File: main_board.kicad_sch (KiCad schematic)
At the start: 13 parts, among them CN2 DF40C-50DP-0.4V, CN20 DF40C-20DP-0.4V, CN5 DF40C-20DP-0.4V, CN7 DF40C-20DP-0.4V, J4 DF40C-100DP-0.4V51, J5 DF40C-100DP-0.4V51, SW1 RESET_L, SW2 PWRON_L, U11 SiP32508DT

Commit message: finished rf sense and io board closure, added audio system with pcm and three spdt switches, made changes tp lte module, added ldo and sd/sim slot, updated m.2/audio schematics, added new mic msop qfn sot footprints, and added a protection system for non EM06-A Cards
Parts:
- removed CN5: DF40C-20DP-0.4V, slate113:CONN-SMD_20P-P0.40_HRS_DF40TC-20DP-0.4V, symbol slate113:DF40C-20DP-0.4V
- added C111, C114, C115, C133, C134, C136, C139: 100nF, symbol Device:C_Small
- added C116, C131, C135, C137, C140: 10µF, symbol Device:C_Small
- added C117, C123: 2.2µF, symbol Device:C_Small
- added C118, C120, C121, C124, C129, C130, C132, C138: 1µF, symbol Device:C_Small
- added C119, C122: 100pF, symbol Device:C_Small
- added C125, C126, C127, C128: 1nF, symbol Device:C_Small
- added CN10: DF40C-40DP-0.4V, slate113:CONN-SMD_DF40C-40DP-0.4V, symbol slate113:DF40C-40DP-0.4V
- added FB6, FB7, FB8, FB9: 600Ω @ 100MHz, symbol Device:FerriteBead_Small
- added LS1, LS2: CES-24205-18-L200, symbol Connector:Conn_01x02_Pin
- added MIC1: MSM381A3729H9CP, slate113:MIC-SMD_4P-L3.8-W3.0-P2.46-S1.70-TR, symbol slate113:MSM381A3729H9CP
- added R67: 33Ω, symbol Device:R_Small
- added R70: 10Ω, symbol Device:R_Small
- added R71, R72, R73: 1kΩ, symbol Device:R_Small
- added R74, R75: 10kΩ, symbol Device:R_Small
- added U47: ES8388, slate113:QFN-28_L4.0-W4.0-P0.45-BL-EP, symbol slate113:ES8388
- added U48, U49: TS5A23157DGSR, slate113:MSOP-10_L3.0-W3.0-P0.50-LS5.0-BL, symbol slate113:TS5A23157DGSR
- added U50, U51: PAM8302AASCR, slate113:MSOP-8_L3.0-W3.0-P0.65-LS5.0-BL, symbol slate113:PAM8302AASCR
- added U52: TPS7A0233PDBVR, slate113:SOT-23-5_L2.9-W1.6-P0.95-LS2.8-BR, symbol slate113:TPS7A0233PDBVR
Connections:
- net FerriteGND_RADIO is gone; now on net FerriteGND_Carrier: CN20.21, CN20.22, CN20.23, CN20.24
- net 1V8: now also C111.1, R71.2, R72.2, U47.2 (DVDD), U47.3 (PVDD), U48.8 (V+), U49.8 (V+)
- net 3V3: now also R73.1
- net CM5_5V: now also C132.2, C136.1, C137.1, C139.1, C140.1, U50.6 (VDD), U51.6 (VDD), U52.1 (IN), U52.3 (EN)
- net CM5_UART_RX: now also J4.95
- net CM5_UART_TX: now also J4.21
- net GND: now also CN2.50, C111.2, C114.2, C115.2, C116.2, C117.2, C118.1, C119.2, C121.1, C122.1, C123.2, C125.2, C126.2, C127.2, C128.2, C131.2, C132.1, C133.2, C134.2, C135.2, C136.2, C137.2, C138.1, C139.2, C140.2, CN10.1, CN10.12, CN10.15, CN10.18, CN10.19, CN10.20, CN10.33, CN10.9, R74.1, R75.1, U47.13 (HPGND), U47.18 (AGND), U47.26 (CE), U47.29 (EP), U47.4 (DGND), U48.3 (GND), U49.3 (GND), U50.4 (IN-), U50.7 (GND), U51.4 (IN-), U51.7 (GND), U52.2 (GND)
- net M2_3V3: now also CN10.2
- net M2_DM: now also CN10.17
- net M2_DP: now also CN10.16
- net M2_PWROFF: now also CN10.3
- net PCIE0_CLKREQ: now also CN10.5
- net PCIE0_PERST: now also CN10.4
- net PCIE0_REFCLKN: now also CN10.8
- net PCIE0_REFCLKP: now also CN10.7
- net PCIE0_RXN: now also CN10.14
- net PCIE0_RXP: now also CN10.13
- net PCIE0_TXN: now also CN10.11
- net PCIE0_TXP: now also CN10.10
- net PCIE0_WAKE: now also CN10.6
- net RADIO_EN: now also J4.27
- net RP_RST: now also J4.25
- net SD_CLK: now also CN10.26
- net SD_CMD: now also CN10.24
- net SD_D0: now also CN10.29
- net SD_D1: now also CN10.28
- net SD_D2: now also CN10.22
- net SD_D3: now also CN10.23
- net SD_PWREN: now also CN10.27
- net WIFI_CTRL: now reaches CN2.45
- net WIFI_CTRL: now also J4.45
- net BLE_CTRL: now reaches CN2.46
- net BLE_CTRL: now also J4.49
- net 5G_SENSE: now reaches CN2.47
- net 5G_SENSE: now also J4.47
- net 2.4G_SENSE: now reaches CN2.48
- net 2.4G_SENSE: now also J4.48
- net BLE_SENSE: now reaches CN2.49
- net BLE_SENSE: now also J4.50
- net AMP_L_SD: now reaches J4.80
- net AMP_L_SD: now also C131.1, C133.1, R74.2, U50.1 (~{SD})
- net AMP_R_SD: now reaches J4.82
- net AMP_R_SD: now also C134.1, C135.1, R75.2, U51.1 (~{SD})
- net CM5_SAI_MCLK: now reaches J4.24
- net CM5_SAI_MCLK: now also R67.1
- net CM5_SAI_SCLK: now reaches J4.26
- net CM5_SAI_SCLK: now also U48.9 (NC1)
- net CM5_SAI_LRCK: now reaches J4.28
- net CM5_SAI_LRCK: now also U48.7 (NC2)
- net CM5_SAI_SDI: now reaches J4.30
- net CM5_SAI_SDI: now also U49.7 (NC2)
- net CM5_SAI_SDO: now reaches J4.34
- net CM5_SAI_SDO: now also U49.9 (NC1)
- net MODEM_AUDIO_EN: now reaches J4.36
- net MODEM_AUDIO_EN: now also CN10.34, U48.1 (IN1), U48.5 (IN2), U49.1 (IN1), U49.5 (IN2)
- new net: C130.1, U50.3 (IN+)
- new net: C120.2, U47.24 (LIN1)
- new net: C118.2, U47.20 (VMID)
- new net: C129.2, U51.3 (IN+)
- new net: R67.2, U47.1 (MCLK)
- new net: C114.1, R70.1, U47.16 (HPVDD)
- new net: C117.1, U47.19 (ADCVREF)
- new net AUDIO_3V3: C115.1, C116.1, C138.2, R70.2, U47.17 (AVDD), U52.5 (OUT)
- new net AUDIO_ASDOUT: U47.8 (ASDOUT), U49.6 (COM2)
- new net AUDIO_DSDIN: U47.6 (DSDIN), U49.10 (COM1)
- new net AUDIO_I2C_SCL: R72.1, U47.28 (CCLK)
- new net AUDIO_I2C_SDA: R71.1, U47.27 (CDATA)
- new net AUDIO_LOUT1: C130.2, U47.12 (LOUT1)
- new net AUDIO_LRCK: U47.7 (LRCK), U48.6 (COM2)
- new net AUDIO_PCM_CLK_F: CN10.21, U48.2 (NO1)
- new net AUDIO_PCM_IN_F: CN10.31, U49.4 (NO2)
- new net AUDIO_PCM_OUT_F: CN10.30, U49.2 (NO1)
- new net AUDIO_PCM_SYNC_F: CN10.32, U48.4 (NO2)
- new net AUDIO_ROUT1: C129.1, U47.11 (ROUT1)
- new net AUDIO_SCLK: U47.5 (SCLK), U48.10 (COM1)
- new net AUDIO_VREF: C121.2, U47.10 (VREF)
- new net MIC_BIAS: C123.1, MIC1.1 (VDD), R73.2
- new net MIC_GND_SENSE: C119.1, MIC1.2 (GND), MIC1.3 (GND), U47.23 (RIN1)
- new net MIC_OUT: C124.1, MIC1.4 (OUT)
- new net MIC_OUT_AC: C120.1, C122.2, C124.2
- new net SD_VDD: CN10.25
- new net SPK_L+: FB6.1, U50.5 (VO+)
- new net SPK_L+_F: C125.1, FB6.2, LS1.1 (Pin_1)
- new net SPK_L-: FB7.1, U50.8 (VO-)
- new net SPK_L-_F: C126.1, FB7.2, LS1.2 (Pin_2)
- new net SPK_R+: FB8.1, U51.5 (VO+)
- new net SPK_R+_F: C127.1, FB8.2, LS2.1 (Pin_1)
- new net SPK_R-: FB9.1, U51.8 (VO-)
- new net SPK_R-_F: C128.1, FB9.2, LS2.2 (Pin_2)
- no-connect marks 114 -> 106
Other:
- note added: "Audio LDO"
- note added: "Ferrite"
- note added: "Stereo Audio Codec Stuff"
- note removed: "Misc"
- moved on the sheet: J4A, J4B

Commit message: finished slateconnect i2c gpio expander, completed led status bar schematic, fixed all drc errors, started assigning footprints and started bom
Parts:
- removed CN20, CN7: DF40C-20DP-0.4V, slate113:CONN-SMD_20P-P0.40_HRS_DF40TC-20DP-0.4V, symbol slate113:DF40C-20DP-0.4V
- added C147, C211, C215, C219: 100nF, Capacitor_SMD:C_0603_1608Metric, symbol Device:C_Small
- added C150, C155: 1µF, Capacitor_SMD:C_0603_1608Metric, symbol Device:C_Small
- added C156: 100pF, Capacitor_SMD:C_0603_1608Metric, symbol Device:C_Small
- added C213: 47µF, symbol Device:C_Small
- added C217: 4.7µF, Capacitor_SMD:C_0603_1608Metric, symbol Device:C_Small
- added CN11: DF40C-30DP-0.4V, slate113:CONN-SMD_30P-P0.40_5001-BM0430-15-00, symbol slate113:DF40C-30DP-0.4V
- added CN19: DF40C-24DP-0.4V, slate113:CONN-SMD_DF40C-24DP-0.4V, symbol slate113:DF40C-24DP-0.4V
- added CN8: DF40C-40DP-0.4V, slate113:CONN-SMD_DF40C-40DP-0.4V, symbol slate113:DF40C-40DP-0.4V
- added FPC1: FPC0.5-24P, slate113:FPC-SMD_P0.50-24P_XJ-FGS, symbol slate113:FPC0.5-24P
- added FPC2: FPC-0.5FX-6PWBH10, slate113:FPC-SMD_FPC-0.5FX-6PWBH10, symbol slate113:FPC-0.5FX-6PWBH10
- added Q4: MMBT3904-C20526, slate113:SOT-23-3_L2.9-W1.3-P1.90-LS2.4-BR, symbol slate113:MMBT3904-C20526
- added R105: 100kΩ, Resistor_SMD:R_0603_1608Metric, symbol Device:R_Small
- added R106, R107: 560Ω, Resistor_SMD:R_0603_1608Metric, symbol Device:R_Small
- added R108, R109, R96: 10kΩ, Resistor_SMD:R_0603_1608Metric, symbol Device:R_Small
- added R97, R98: 4.7kΩ, Resistor_SMD:R_0603_1608Metric, symbol Device:R
- added R99: 200kΩ, Resistor_SMD:R_0603_1608Metric, symbol Device:R_Small
- added U62: PCA9306DCUR, slate113:SSOP-8_L2.0-W2.3-P0.50-LS3.1-BR, symbol slate113:PCA9306DCUR
- added U63: AP2120N-2.8TRG1, slate113:SOT-23-3_L2.9-W1.3-P1.90-LS2.4-BR, symbol slate113:AP2120N-2.8TRG1
- added U66: DF40B-10DS-0.4V, slate113:CONN-SMD_10P-P0.40_DF40B-10DS-0.4V-51, symbol slate113:DF40B-10DS-0.4V
- added U67: SIP32508DT-T1-GE3, slate113:TSOT-23-6_L2.9-W1.6-P0.95-LS2.8-BR, symbol slate113:SIP32508DT-T1-GE3
- added U68: SN74AHCT125PWR, slate113:TSSOP-14_L5.0-W4.4-P0.65-LS6.4-BL, symbol slate113:SN74AHCT125PWR
- added U8: ESD7104MUTAG_C2987068, slate113:DFN-10_L2.5-W1.0-P0.50-BL, symbol slate113:ESD7104MUTAG_C2987068
- C111, C114, C115, C133, C134, C136, C139, C21: footprint (none) -> Capacitor_SMD:C_0603_1608Metric; MPN (none) -> CL10B104KB8NNNC; Manufacturer (none) -> Samsung Electro-Mechanics
- C116, C131, C135, C137, C140: footprint (none) -> Capacitor_SMD:C_0603_1608Metric; MPN (none) -> CL10A106KP8NNNC; Manufacturer (none) -> Samsung Electro-Mechanics
- C117, C123, C19: footprint (none) -> Capacitor_SMD:C_0603_1608Metric; MPN (none) -> CL10B225KA8NNNC; Manufacturer (none) -> Samsung Electro-Mechanics
- C118, C120, C121, C124, C129, C130, C132, C138: footprint (none) -> Capacitor_SMD:C_0603_1608Metric; MPN (none) -> CL10B105KA8NNNC; Manufacturer (none) -> Samsung Electro-Mechanics
- C119, C122: footprint (none) -> Capacitor_SMD:C_0603_1608Metric; MPN (none) -> CL10C101JB8NNNC; Manufacturer (none) -> Samsung Electro-Mechanics
- C125, C126, C127, C128: footprint (none) -> Capacitor_SMD:C_0603_1608Metric; MPN (none) -> CL10B102KB8NNNC; Manufacturer (none) -> Samsung Electro-Mechanics
- J4: MPN (none) -> DF40C-100DP-0.4V51; Manufacturer (none) -> LCSC
- R17: footprint (none) -> Resistor_SMD:R_0603_1608Metric; MPN (none) -> RC0603FR-07100KL; Manufacturer (none) -> Yageo
- R67: footprint (none) -> Resistor_SMD:R_0603_1608Metric; MPN (none) -> RC0603FR-0733RL; Manufacturer (none) -> Yageo
- R70: footprint (none) -> Resistor_SMD:R_0603_1608Metric; MPN (none) -> RC0603FR-0710RL; Manufacturer (none) -> Yageo
- R71, R72, R73: footprint (none) -> Resistor_SMD:R_0603_1608Metric; MPN (none) -> RC0603FR-071KL; Manufacturer (none) -> Yageo
- R74, R75: footprint (none) -> Resistor_SMD:R_0603_1608Metric; MPN (none) -> RC0603FR-0710KL; Manufacturer (none) -> Yageo
- SW1: MPN (none) -> C&K KMR231GLFS; Manufacturer (none) -> C&K
- SW2: MPN (none) -> C&K KMR231GLFS; Manufacturer (none) -> DigiKey
- U11: MPN (none) -> SiP32508DT; Manufacturer (none) -> LCSC
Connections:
- net 1V8: now also CN11.5, FPC1.22, R96.1, R97.2, R98.1, U62.2 (VREF1)
- net 3V3: now also C150.1, CN11.4, CN19.14, CN8.11, FPC1.23, R99.2, U63.3 (VIN)
- net 5V: now also CN19.12
- net BQ_INT: now also CN11.7
- net CM5_5V: now also C215.1, C217.1, C219.1, CN11.2, CN11.3, R109.2, U67.5 (IN), U67.6 (IN), U68.10 (~{3OE}), U68.13 (~{4OE}), U68.14 (VCC)
- net CM5_UART_RX: now also CN19.17
- net CM5_UART_TX: now also CN19.19
- net FerriteGND_Carrier: now also CN10.41, CN10.42, CN10.43, CN10.44, CN11.31, CN11.32, CN11.33, CN11.34, CN19.25, CN19.26, CN19.27, CN19.28
- net GND: now also C147.2, C150.2, C155.1, C156.2, C211.2, C213.2, C215.2, C217.2, C219.2, CN11.1, CN11.11, CN11.12, CN11.6, CN19.10, CN19.11, CN19.16, CN19.18, CN19.20, CN19.24, CN19.9, CN8.1, CN8.2, CN8.3, CN8.4, CN8.41, CN8.42, CN8.43, CN8.44, FPC1.11, FPC1.14, FPC1.17, FPC1.2, FPC1.24, FPC1.25, FPC1.26, FPC1.5, FPC1.8, FPC2.6, FPC2.7, FPC2.8, Q4.2 (E), R105.2, U62.1 (GND), U63.1 (GND), U66.11, U66.12, U66.13, U66.14, U66.2, U66.4, U66.5, U66.8, U67.4 (GND), U68.12 (4A), U68.7 (GND), U68.9 (3A), U8.3, U8.8
- net I2C0_SCL: now also CN11.8, CN8.13, U62.6 (SCL2)
- net I2C0_SDA: now also CN11.9, CN8.12, U62.5 (SDA2)
- net MODEM_AUDIO_EN: now also J4.91; no longer J4.36
- net RADIO_EN: now also J4.89, CN19.13; no longer J4.27
- net RP_RST: now also J4.97, CN19.15; no longer J4.25
- net SD_CLK: no longer CN2.19
- net SD_CMD: no longer CN2.20
- net SD_D0: no longer CN2.21
- net SD_D1: no longer CN2.22
- net SD_D2: no longer CN2.23
- net SD_D3: no longer CN2.24
- net SD_DET: no longer CN2.25
- net SD_PWREN: no longer CN2.18
- net DSI_D0N: now reaches J5.75
- net DSI_D0N: now also FPC1.6
- net DSI_D0P: now reaches J5.77
- net DSI_D0P: now also FPC1.7
- net DSI_D1N: now reaches J5.81
- net DSI_D1N: now also FPC1.12
- net DSI_D1P: now reaches J5.83
- net DSI_D1P: now also FPC1.13
- net DSI_CLKN: now reaches J5.87
- net DSI_CLKN: now also FPC1.9
- net DSI_CLKP: now reaches J5.89
- net DSI_CLKP: now also FPC1.10
- net DSI_D2N: now reaches J5.93
- net DSI_D2N: now also FPC1.15
- net DSI_D3N: now reaches J5.94
- net DSI_D3N: now also FPC1.3
- net DSI_D2P: now reaches J5.95
- net DSI_D2P: now also FPC1.16
- net DSI_D3P: now reaches J5.96
- net DSI_D3P: now also FPC1.4
- net CM5_ACC_RESET_N: now reaches J4.54
- net CM5_ACC_RESET_N: now also CN8.27
- net CM5_ACC_AUX0: now reaches J4.56
- net CM5_ACC_AUX0: now also CN8.28
- net CM5_ACC_MISO: now reaches J4.29
- net CM5_ACC_MISO: now also CN8.24
- net CM5_ACC_CS0_N: now reaches J4.31
- net CM5_ACC_CS0_N: now also CN8.25
- net CM5_ACC_IRQ0: now reaches J4.35
- net CM5_ACC_IRQ0: now also CN8.26
- net LCD_RST_L: now reaches J4.39
- net LCD_RST_L: now also C147.1, FPC1.19, R96.2
- new net: C156.1, R99.1, U62.7 (VREF2), U62.8 (EN)
- new net CM5_ACC_AUX1: CN8.29, J4.36
- new net CM5_ACC_MOSI: CN8.23, J4.27
- new net CM5_ACC_SCK: CN8.22, J4.25
- new net LCD_LED_A: CN11.20, FPC1.21
- new net LCD_LED_K: CN11.21, FPC1.20
- new net LCD_PWM: CN11.19, FPC1.18
- new net LED_5V: C211.1, C213.1, U66.1, U66.10, U66.3, U66.9, U67.1 (OUT), U67.2 (OUT)
- new net LED_BUF_BASE: Q4.1 (B), R108.1
- new net LED_BUF_OE_N: Q4.3 (C), R109.1, U68.1 (~{1OE}), U68.4 (~{2OE})
- new net LED_CLK_3V3: CN19.22, U68.5 (2A)
- new net LED_CLK_5V: R107.1, U68.6 (2Y)
- new net LED_CLK_IN: R107.2, U66.6
- new net LED_DATA_3V3: CN19.21, U68.2 (1A)
- new net LED_DATA_5V: R106.1, U68.3 (1Y)
- new net LED_DATA_IN: R106.2, U66.7
- new net LED_PWR_EN: CN19.23, R105.1, R108.2, U67.3 (EN)
- new net RP_ACC_AUX0: CN19.1, CN8.36
- new net RP_ACC_AUX1: CN19.2, CN8.37
- new net RP_ACC_CS0_N: CN19.6, CN8.33
- new net RP_ACC_IRQ0: CN19.3, CN8.34
- new net RP_ACC_MISO: CN19.5, CN8.32
- new net RP_ACC_MOSI: CN19.8, CN8.31
- new net RP_ACC_RESET_N: CN19.4, CN8.35
- new net RP_ACC_SCK: CN19.7, CN8.30
- new net SC_SEL0: CN8.14
- new net SC_SEL1: CN8.15
- new net SC_SEL2: CN8.16
- new net SC_SEL3: CN8.17
- new net SC_SEL4: CN8.18
- new net SC_SEL5: CN8.19
- new net SC_SEL6: CN8.20
- new net SC_SEL7: CN8.21
- new net TP_2V8: C155.2, FPC2.1, U63.2 (VOUT)
- new net TP_INT_L: FPC2.5, U8.5
- new net TP_RST_L: FPC2.3, U8.2
- new net TP_SCL_1V8: FPC2.2, R98.2, U62.3 (SCL1), U8.1
- new net TP_SDA_1V8: FPC2.4, R97.1, U62.4 (SDA1), U8.4
- new net VBUS: CN11.13, CN11.14, CN11.15, CN8.5, CN8.6, CN8.7
- new net VIN_EXT: CN11.16, CN11.17, CN11.18, CN8.10, CN8.8, CN8.9
- no-connect marks 106 -> 99
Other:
- note added: "2V8 LDO"
- note added: "B2B > Carrier"
- note added: "Buffer"
- note added: "Carrier -> LED Status"
- note added: "Display Clamshell"
- note added: "Level Shifter"
- note added: "MOSFET"
- note added: "Power Distributor"
- note added: "TVS"
- note added: "Touch Clamshell"
- moved on the sheet: J4B

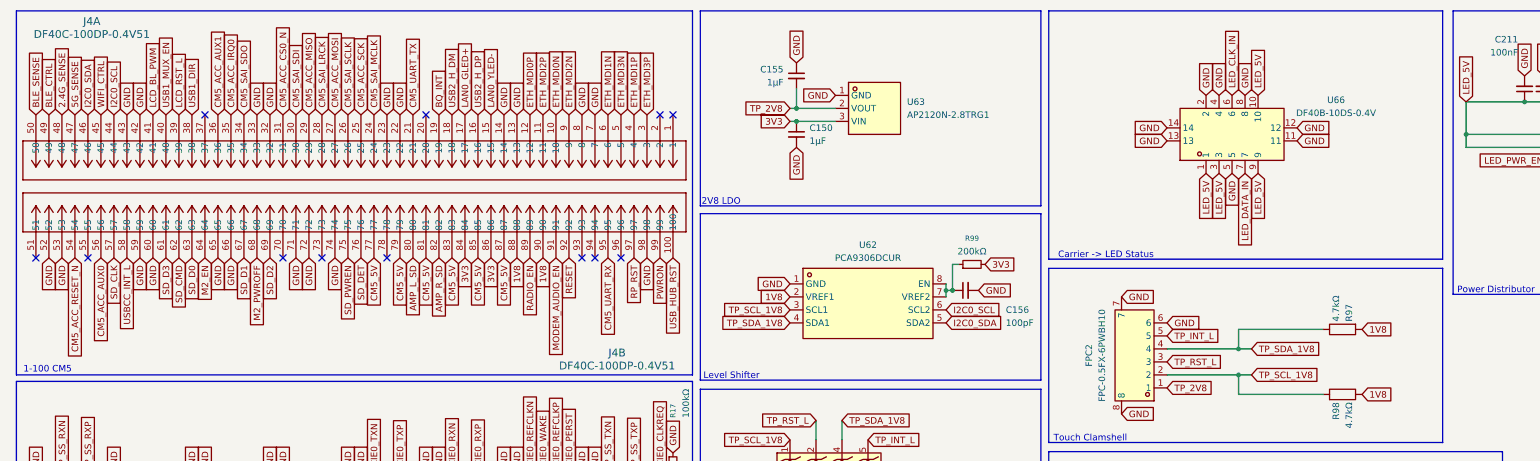
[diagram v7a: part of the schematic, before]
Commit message: assigned footprints and mpns across schematics + added 3d models and footprint libraries
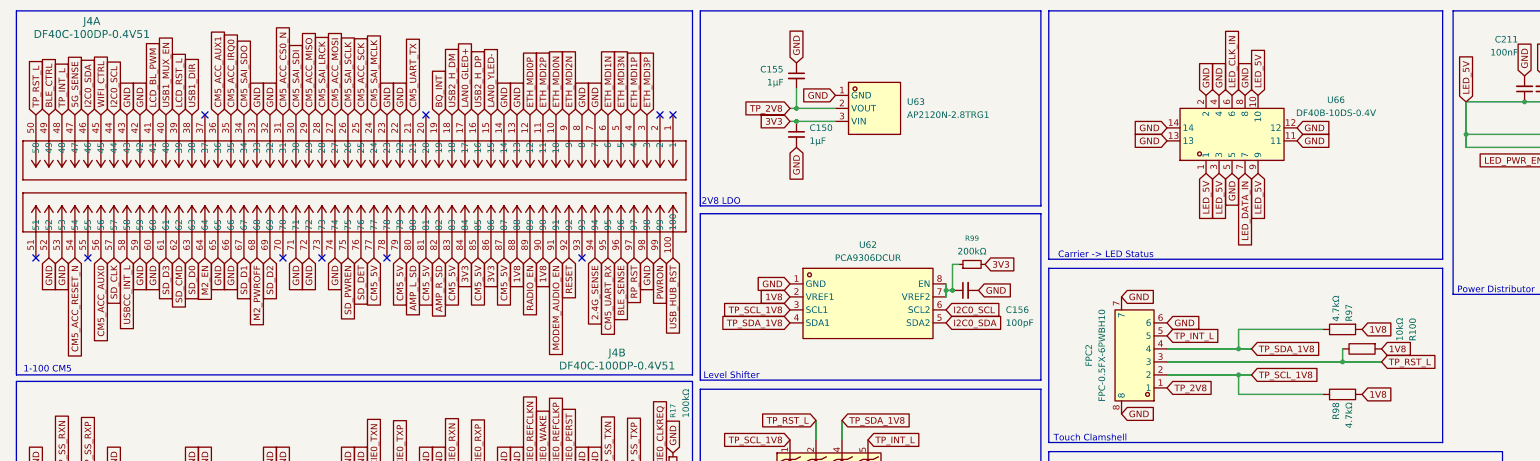
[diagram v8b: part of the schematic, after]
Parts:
- added R100: 10kΩ, Resistor_SMD:R_0603_1608Metric, symbol Device:R
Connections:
- net 1V8: now also R100.2
- net 2.4G_SENSE: now also J4.94; no longer J4.48
- net BLE_SENSE: now also J4.96; no longer J4.50
- net TP_INT_L: now also J4.48
- net TP_RST_L: now also J4.50, R100.1
- no-connect marks 99 -> 97
